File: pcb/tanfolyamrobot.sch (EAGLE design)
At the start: 79 parts, among them IC1 STM32F10XRXT6, IC2 7805, IC4 FT232RL, IC5 LD117AS33TR, M1 DRV8833, Q1 16MHz, Q2 BSS123, Q3 BSS123, Q4 BSS123, X2 PWR, X6 KUSBVX-BS1N

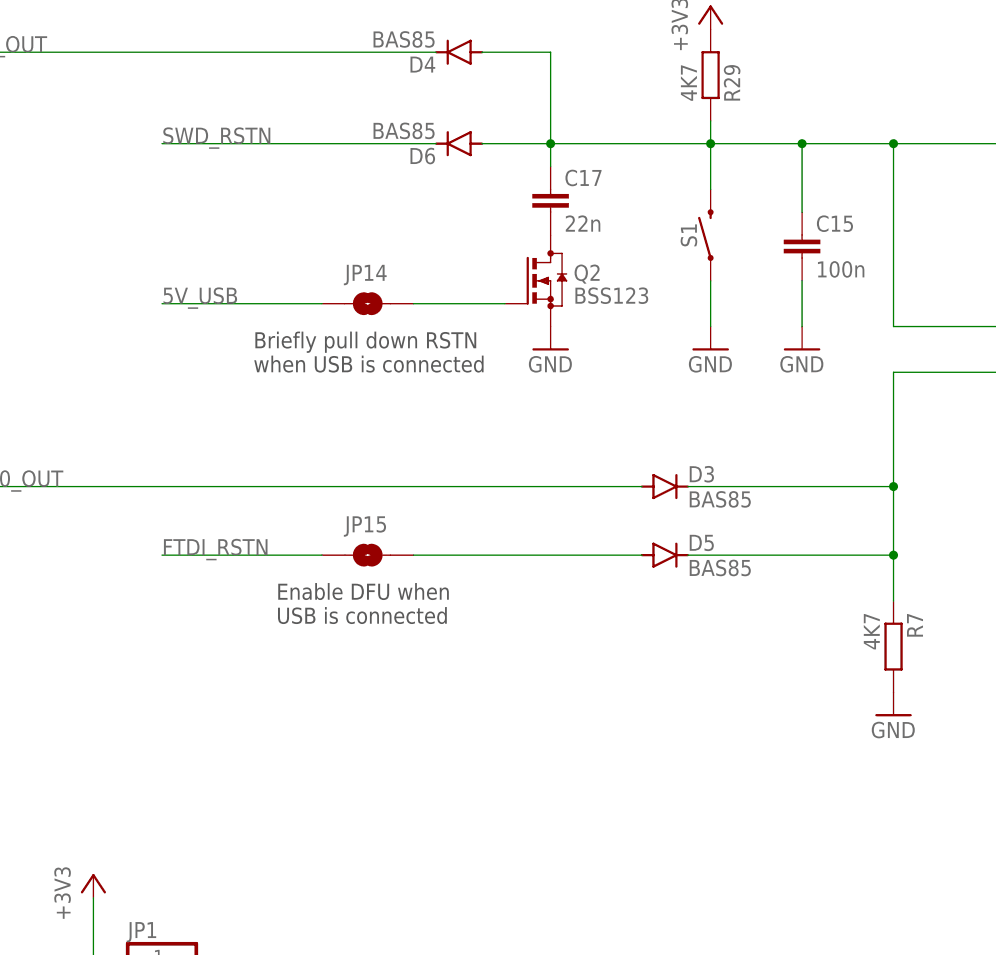
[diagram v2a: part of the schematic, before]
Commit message: moved 5V_USB reset's cap to the gate of the mosfet (#1)
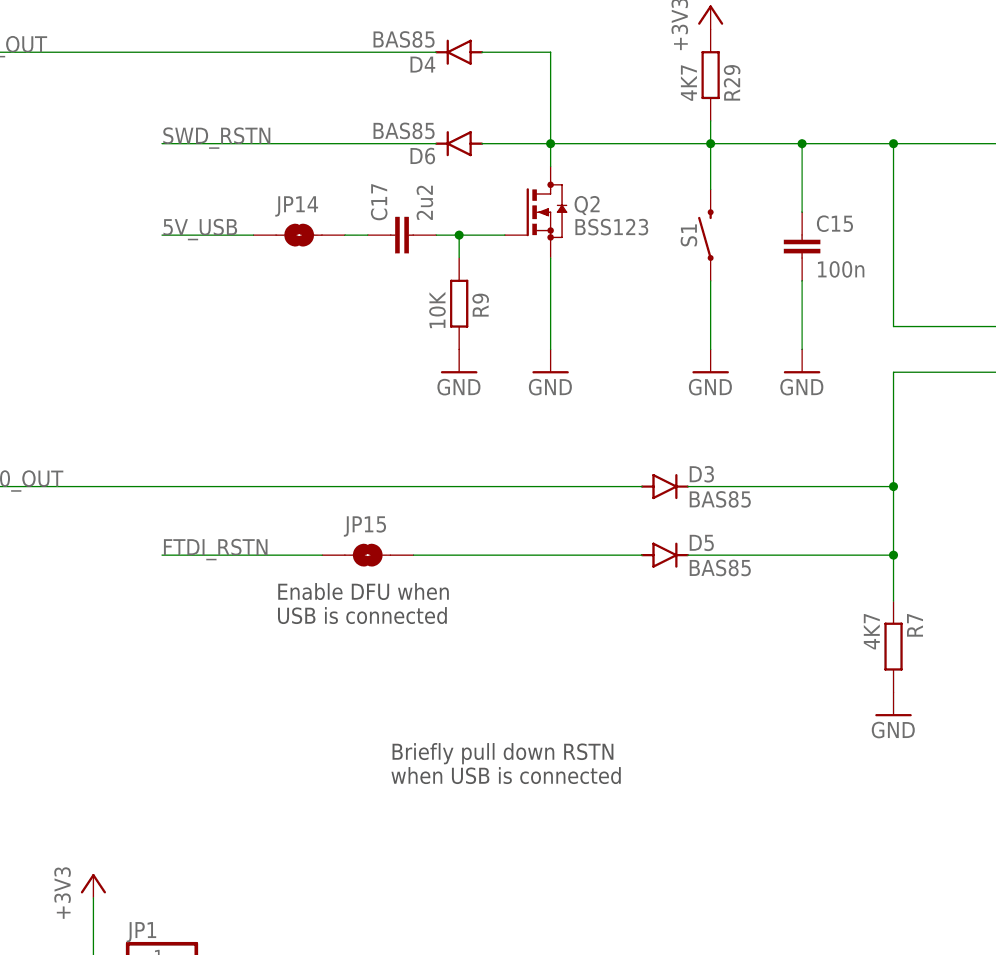
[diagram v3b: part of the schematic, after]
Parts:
- added R9: 10K, rcl:R-EU_R0603
- C17: value 22n -> 2u2
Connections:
- removed net N$6: JP14.2, Q2.G
- removed net N$9: C17.2, Q2.D
- new net N$2: C17.2, Q2.G, R9.1
- new net N$4: C17.1, JP14.2
- net GND: now also R9.2
- net RSTN: now also Q2.D; no longer C17.1
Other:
- moved on the sheet: C17, JP14, Q2
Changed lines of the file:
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@@
 <part name="+3V11" library="supply1" library_urn="urn:adsk.eagle:library:371" deviceset="+3V3" device=""/>
 <part name="D3" library="diode" library_urn="urn:adsk.eagle:library:210" deviceset="DIODE-" device="MICROMELF-W" package3d_urn="urn:adsk.eagle:package:43441/2" value="BAS85"/>
-<part name="C17" library="rcl" library_urn="urn:adsk.eagle:library:334" deviceset="C-EU" device="C0603" package3d_urn="urn:adsk.eagle:package:23616/2" value="22n"/>
 <part name="D4" library="diode" library_urn="urn:adsk.eagle:library:210" deviceset="DIODE-" device="MICROMELF-W" package3d_urn="urn:adsk.eagle:package:43441/2" value="BAS85"/>
 <part name="D6" library="diode" library_urn="urn:adsk.eagle:library:210" deviceset="DIODE-" device="MICROMELF-W" package3d_urn="urn:adsk.eagle:package:43441/2" value="BAS85"/>
@@
 <part name="C15" library="rcl" library_urn="urn:adsk.eagle:library:334" deviceset="C-EU" device="C0603" package3d_urn="urn:adsk.eagle:package:23616/2" value="100n"/>
 <part name="GND33" library="supply1" library_urn="urn:adsk.eagle:library:371" deviceset="GND" device=""/>
+<part name="C17" library="rcl" library_urn="urn:adsk.eagle:library:334" deviceset="C-EU" device="C0603" package3d_urn="urn:adsk.eagle:package:23616/2" value="2u2"/>
+<part name="R9" library="rcl" library_urn="urn:adsk.eagle:library:334" deviceset="R-EU_" device="R0603" package3d_urn="urn:adsk.eagle:package:23555/3" value="10K"/>
+<part name="GND35" library="supply1" library_urn="urn:adsk.eagle:library:371" deviceset="GND" device=""/>
 </parts>
 <sheets>
@@
 FTDI</text>
 <text x="353.06" y="25.4" size="1.778" layer="97">COLOR_OEn</text>
-<text x="129.54" y="299.72" size="1.778" layer="97">Briefly pull down RSTN
+<text x="144.78" y="254" size="1.778" layer="97">Briefly pull down RSTN
 when USB is connected</text>
 <text x="132.08" y="271.78" size="1.778" layer="97">Enable DFU when
@@
 <attribute name="VALUE" x="374.65" y="132.08" size="1.778" layer="96" rot="MR180"/>
 </instance>
-<instance part="Q2" gate="G$1" x="162.56" y="309.88" smashed="yes">
-<attribute name="NAME" x="165.1" y="309.88" size="1.778" layer="95"/>
-<attribute name="VALUE" x="165.1" y="307.34" size="1.778" layer="96"/>
-</instance>
-<instance part="GND18" gate="1" x="162.56" y="302.26" smashed="yes">
-<attribute name="VALUE" x="160.02" y="299.72" size="1.778" layer="96"/>
+<instance part="Q2" gate="G$1" x="162.56" y="317.5" smashed="yes">
+<attribute name="NAME" x="165.1" y="317.5" size="1.778" layer="95"/>
+<attribute name="VALUE" x="165.1" y="314.96" size="1.778" layer="96"/>
+</instance>
+<instance part="GND18" gate="1" x="162.56" y="299.72" smashed="yes">
+<attribute name="VALUE" x="160.02" y="297.18" size="1.778" layer="96"/>
 </instance>
 <instance part="C16" gate="G$1" x="330.2" y="157.48" smashed="yes">
@@
 <attribute name="VALUE" x="180.848" y="314.96" size="1.778" layer="96" font="vector" rot="R90" align="top-center"/>
 </instance>
-<instance part="GND26" gate="1" x="180.34" y="302.26" smashed="yes">
-<attribute name="VALUE" x="177.8" y="299.72" size="1.778" layer="96"/>
+<instance part="GND26" gate="1" x="180.34" y="299.72" smashed="yes">
+<attribute name="VALUE" x="177.8" y="297.18" size="1.778" layer="96"/>
 </instance>
 <instance part="S2" gate="G$1" x="292.1" y="215.9" smashed="yes" rot="R90">
@@
 <attribute name="VALUE" x="177.8" y="284.7086" size="1.778" layer="96"/>
 </instance>
-<instance part="C17" gate="G$1" x="162.56" y="320.04" smashed="yes">
-<attribute name="NAME" x="164.084" y="320.421" size="1.778" layer="95"/>
-<attribute name="VALUE" x="164.084" y="315.341" size="1.778" layer="96"/>
-</instance>
 <instance part="D4" gate="G$1" x="152.4" y="335.28" smashed="yes" rot="R180">
 <attribute name="NAME" x="149.86" y="334.7974" size="1.778" layer="95" rot="R180"/>
@@
 <attribute name="NAME" x="60.96" y="279.4" size="1.778" layer="95" font="vector"/>
 </instance>
-<instance part="JP14" gate="G$1" x="142.24" y="307.34" smashed="yes">
-<attribute name="NAME" x="139.7" y="309.88" size="1.778" layer="95" font="vector"/>
+<instance part="JP14" gate="G$1" x="134.62" y="314.96" smashed="yes">
+<attribute name="NAME" x="132.08" y="317.5" size="1.778" layer="95" font="vector"/>
 </instance>
 <instance part="JP15" gate="G$1" x="142.24" y="279.4" smashed="yes">
@@
 <attribute name="VALUE" x="192.024" y="310.261" size="1.778" layer="96"/>
 </instance>
-<instance part="GND33" gate="1" x="190.5" y="302.26" smashed="yes">
-<attribute name="VALUE" x="187.96" y="299.72" size="1.778" layer="96"/>
+<instance part="GND33" gate="1" x="190.5" y="299.72" smashed="yes">
+<attribute name="VALUE" x="187.96" y="297.18" size="1.778" layer="96"/>
+</instance>
+<instance part="C17" gate="G$1" x="144.78" y="314.96" smashed="yes" rot="R90">
+<attribute name="NAME" x="144.399" y="316.484" size="1.778" layer="95" rot="R90"/>
+<attribute name="VALUE" x="149.479" y="316.484" size="1.778" layer="96" rot="R90"/>
+</instance>
+<instance part="R9" gate="G$1" x="152.4" y="307.34" smashed="yes" rot="R270">
+<attribute name="NAME" x="153.8986" y="308.61" size="1.778" layer="95" rot="R270"/>
+<attribute name="VALUE" x="149.098" y="308.61" size="1.778" layer="96" rot="R270"/>
+</instance>
+<instance part="GND35" gate="1" x="152.4" y="299.72" smashed="yes">
+<attribute name="VALUE" x="149.86" y="297.18" size="1.778" layer="96"/>
 </instance>
 </instances>
@@
 <pinref part="Q2" gate="G$1" pin="S"/>
 <pinref part="GND18" gate="1" pin="GND"/>
+<wire x1="162.56" y1="312.42" x2="162.56" y2="302.26" width="0.1524" layer="91"/>
 </segment>
 <segment>
@@
 <pinref part="S1" gate="G$1" pin="1"/>
 <pinref part="GND26" gate="1" pin="GND"/>
-<wire x1="180.34" y1="304.8" x2="180.34" y2="309.88" width="0.1524" layer="91"/>
+<wire x1="180.34" y1="302.26" x2="180.34" y2="309.88" width="0.1524" layer="91"/>
 </segment>
 <segment>
@@
 <pinref part="C15" gate="G$1" pin="2"/>
 <pinref part="GND33" gate="1" pin="GND"/>
-<wire x1="190.5" y1="304.8" x2="190.5" y2="309.88" width="0.1524" layer="91"/>
+<wire x1="190.5" y1="302.26" x2="190.5" y2="309.88" width="0.1524" layer="91"/>
+</segment>
+<segment>
+<pinref part="R9" gate="G$1" pin="2"/>
+<pinref part="GND35" gate="1" pin="GND"/>
 </segment>
 </net>
@@
 </segment>
 <segment>
-<wire x1="137.16" y1="307.34" x2="119.38" y2="307.34" width="0.1524" layer="91"/>
-<label x="119.38" y="307.34" size="1.778" layer="95"/>
+<wire x1="129.54" y1="314.96" x2="119.38" y2="314.96" width="0.1524" layer="91"/>
+<label x="119.38" y="314.96" size="1.778" layer="95"/>
 <pinref part="JP14" gate="G$1" pin="1"/>
 </segment>
@@
 <pinref part="R29" gate="G$1" pin="2"/>
 <wire x1="180.34" y1="325.12" x2="180.34" y2="327.66" width="0.1524" layer="91"/>
-<pinref part="C17" gate="G$1" pin="1"/>
 <wire x1="162.56" y1="322.58" x2="162.56" y2="325.12" width="0.1524" layer="91"/>
 <junction x="162.56" y="325.12"/>
@@
 <wire x1="190.5" y1="317.5" x2="190.5" y2="325.12" width="0.1524" layer="91"/>
 <junction x="190.5" y="325.12"/>
+<pinref part="Q2" gate="G$1" pin="D"/>
 </segment>
 <segment>
@@
 <wire x1="474.98" y1="254" x2="457.2" y2="254" width="0.1524" layer="91"/>
 <label x="457.2" y="254" size="1.778" layer="95"/>
-</segment>
-</net>
-<net name="N$6" class="0">
-<segment>
-<pinref part="Q2" gate="G$1" pin="G"/>
-<wire x1="147.32" y1="307.34" x2="157.48" y2="307.34" width="0.1524" layer="91"/>
-<pinref part="JP14" gate="G$1" pin="2"/>
 </segment>
 </net>
@@
 </segment>
 </net>
-<net name="N$9" class="0">
-<segment>
-<pinref part="Q2" gate="G$1" pin="D"/>
-<pinref part="C17" gate="G$1" pin="2"/>
-</segment>
-</net>
 <net name="ESP_TX" class="0">
 <segment>
@@
 </segment>
 </net>
+<net name="N$2" class="0">
+<segment>
+<pinref part="C17" gate="G$1" pin="2"/>
+<wire x1="149.86" y1="314.96" x2="152.4" y2="314.96" width="0.1524" layer="91"/>
+<pinref part="R9" gate="G$1" pin="1"/>
+<wire x1="152.4" y1="314.96" x2="157.48" y2="314.96" width="0.1524" layer="91"/>
+<wire x1="152.4" y1="312.42" x2="152.4" y2="314.96" width="0.1524" layer="91"/>
+<junction x="152.4" y="314.96"/>
+<pinref part="Q2" gate="G$1" pin="G"/>
+</segment>
+</net>
+<net name="N$4" class="0">
+<segment>
+<pinref part="C17" gate="G$1" pin="1"/>
+<wire x1="142.24" y1="314.96" x2="139.7" y2="314.96" width="0.1524" layer="91"/>
+<pinref part="JP14" gate="G$1" pin="2"/>
+</segment>
+</net>

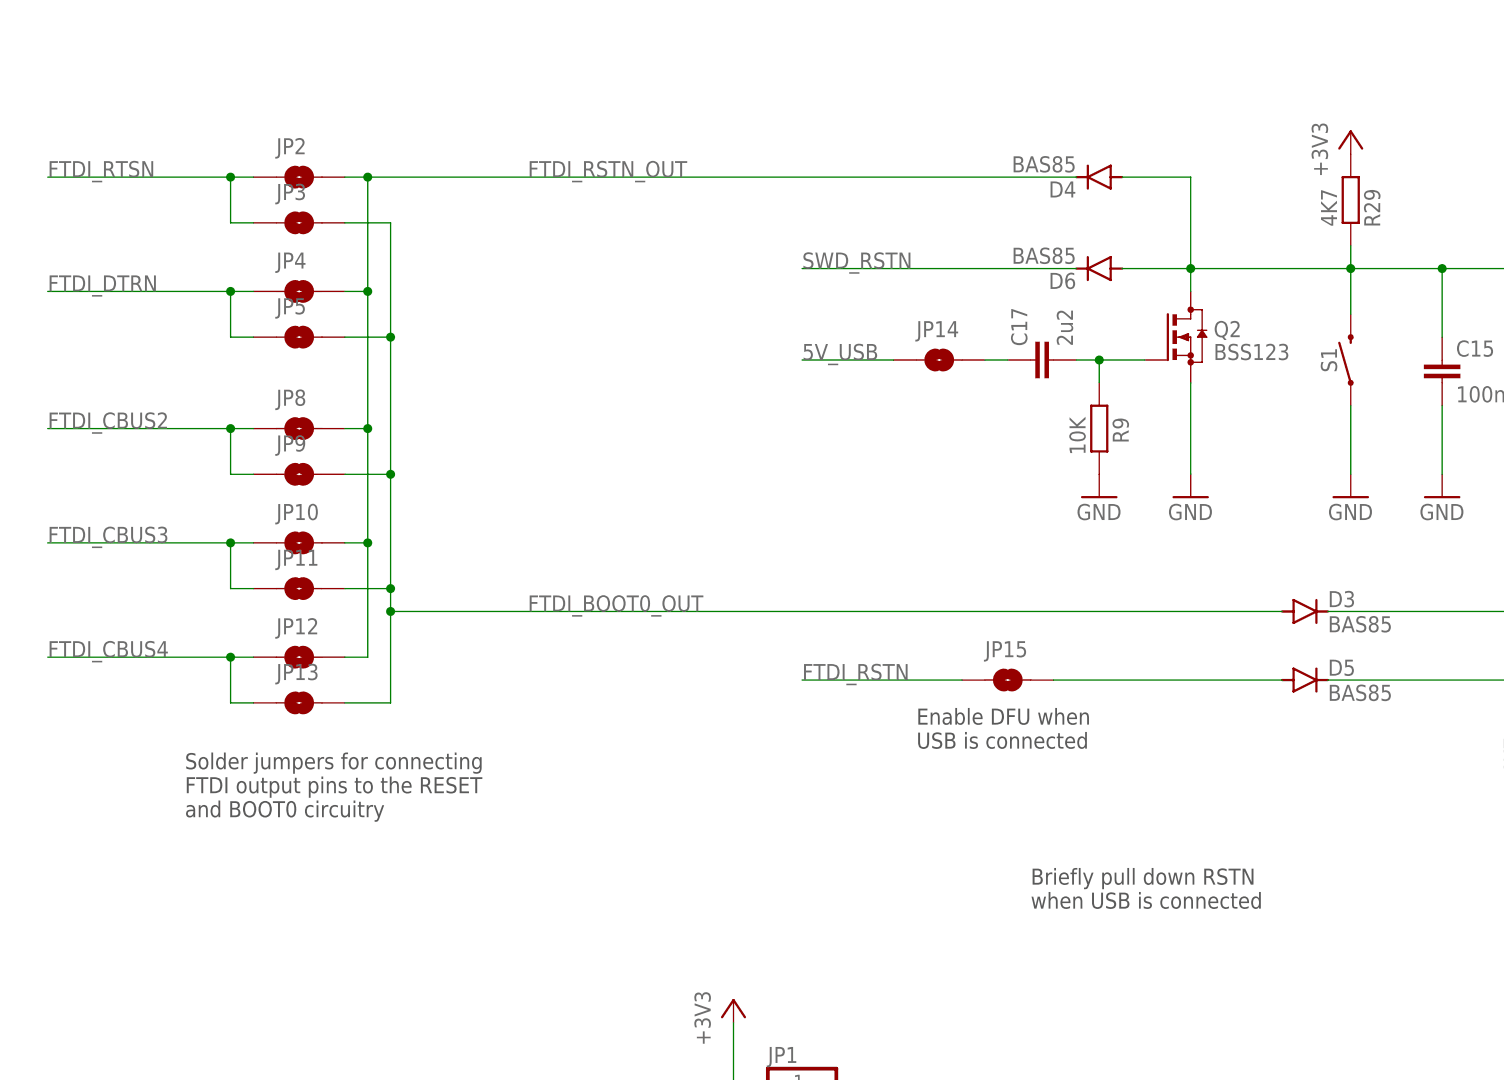
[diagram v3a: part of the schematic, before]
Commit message: changed all solder jumpers to resistors (#1)
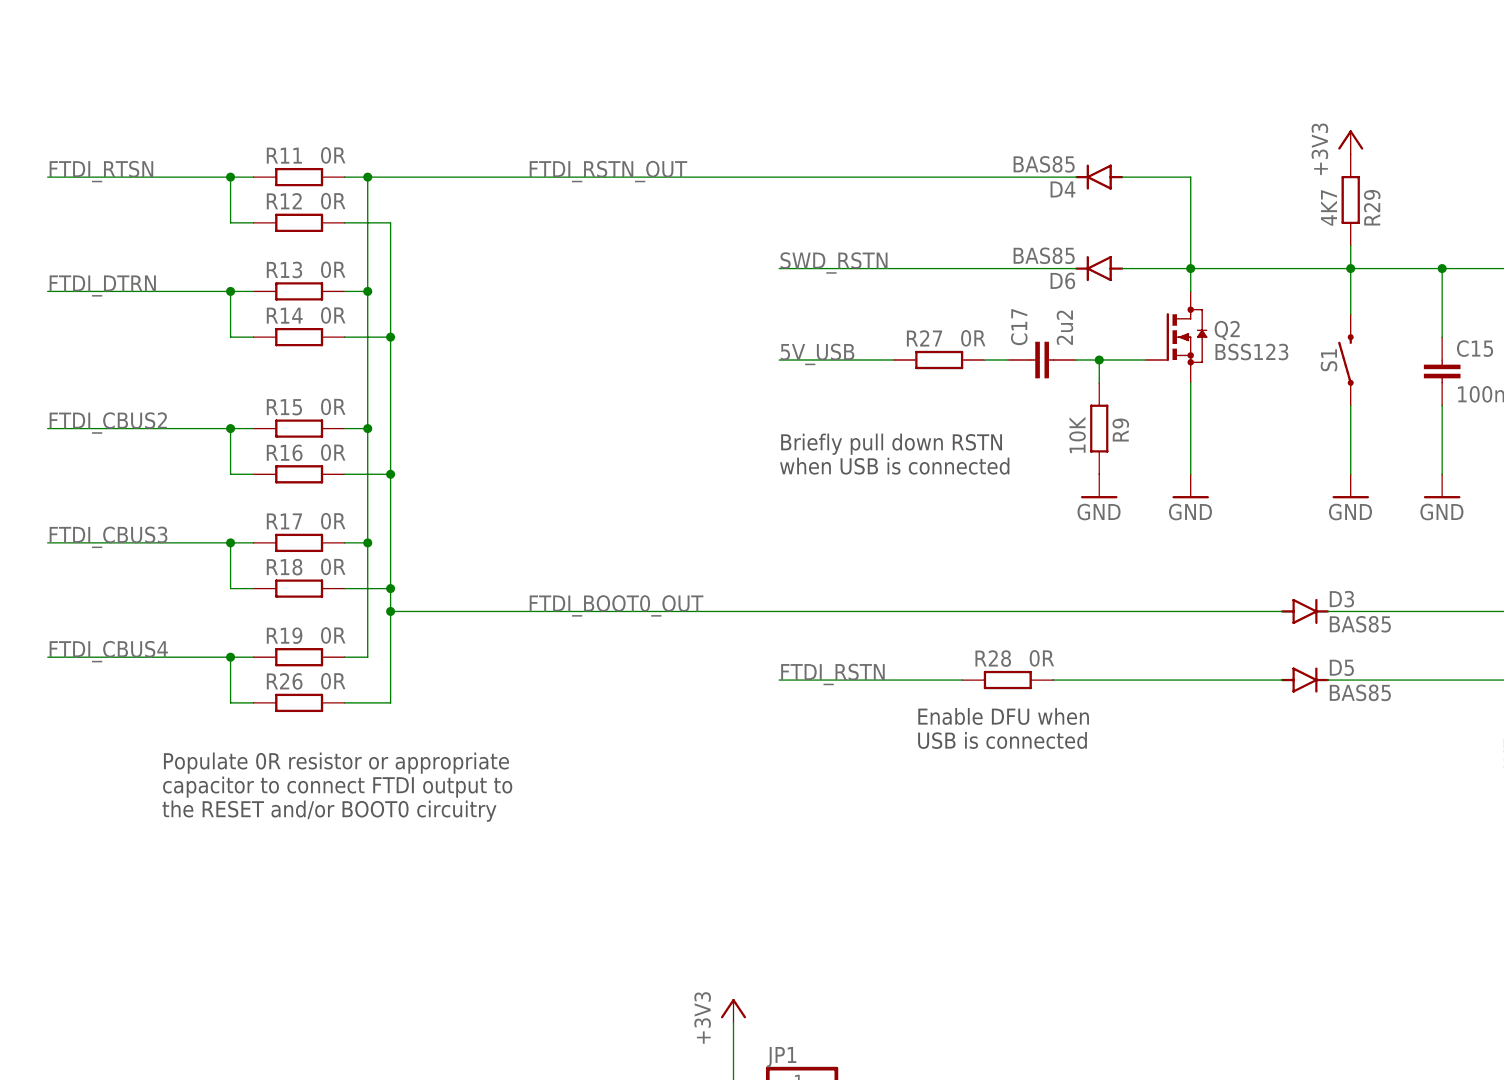
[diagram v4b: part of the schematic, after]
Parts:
- removed JP10, JP11, JP12, JP13, JP14, JP15, JP2, JP3, JP4, JP5, JP8, JP9: JUMPER-SMT_2_NO_NO-SILK, SparkFun-Jumpers:JUMPER-SMT_2_NO_NO-SILK
- added R11, R12, R13, R14, R15, R16, R17, R18, R19, R26, R27, R28: 0R, rcl:R-EU_R0603
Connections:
- net 5V_USB: now also R27.1; no longer JP14.1
- net FTDI_BOOT0_OUT: now also R12.2, R14.2, R16.2, R18.2, R26.2; no longer JP11.2, JP13.2, JP3.2, JP5.2, JP9.2
- net FTDI_CBUS2: now also R15.1, R16.1; no longer JP8.1, JP9.1
- net FTDI_CBUS3: now also R17.1, R18.1; no longer JP10.1, JP11.1
- net FTDI_CBUS4: now also R19.1, R26.1; no longer JP12.1, JP13.1
- net FTDI_DTRN: now also R13.1, R14.1; no longer JP4.1, JP5.1
- net FTDI_RSTN: now also R28.1; no longer JP15.1
- net FTDI_RSTN_OUT: now also R11.2, R13.2, R15.2, R17.2, R19.2; no longer JP10.2, JP12.2, JP2.2, JP4.2, JP8.2
- net FTDI_RTSN: now also R11.1, R12.1; no longer JP2.1, JP3.1
- net N$4: now also R27.2; no longer JP14.2
- net N$8: now also R28.2; no longer JP15.2
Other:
- note added: "Populate 0R resistor or appropriate capacitor to connect FTDI output to the RESET and/or BOOT0 circuitry"
- note removed: "Solder jumpers for connecting FTDI output pins to the RESET and BOOT0 circuitry"
